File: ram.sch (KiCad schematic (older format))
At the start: 20 parts, among them U16 XX4256, U17 XX4256, U18 XX4256, U19 XX4256, U20 XX4256, U21 XX4256, U22 XX4256, U23 XX4256, U32 74LS139, U34 74LS373, U35 74LS244

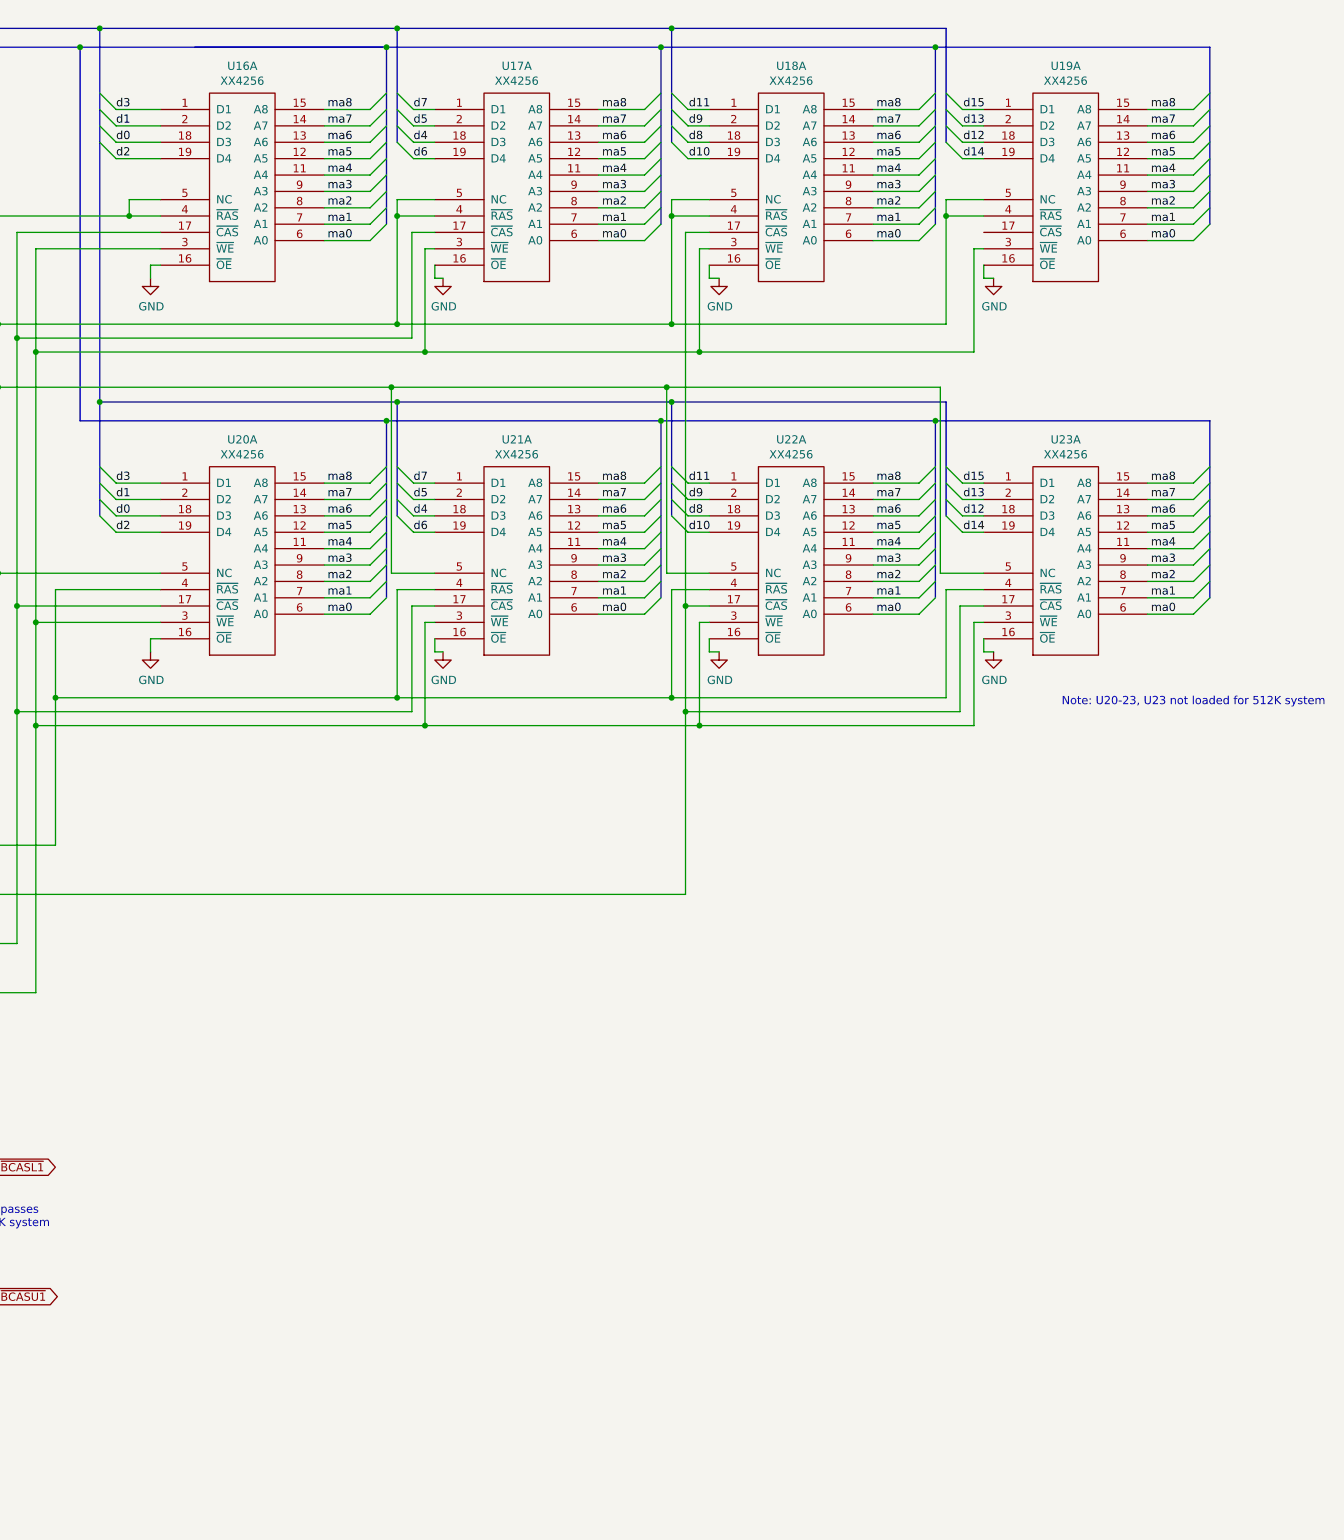
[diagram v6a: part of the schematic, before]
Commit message: Complete RAM
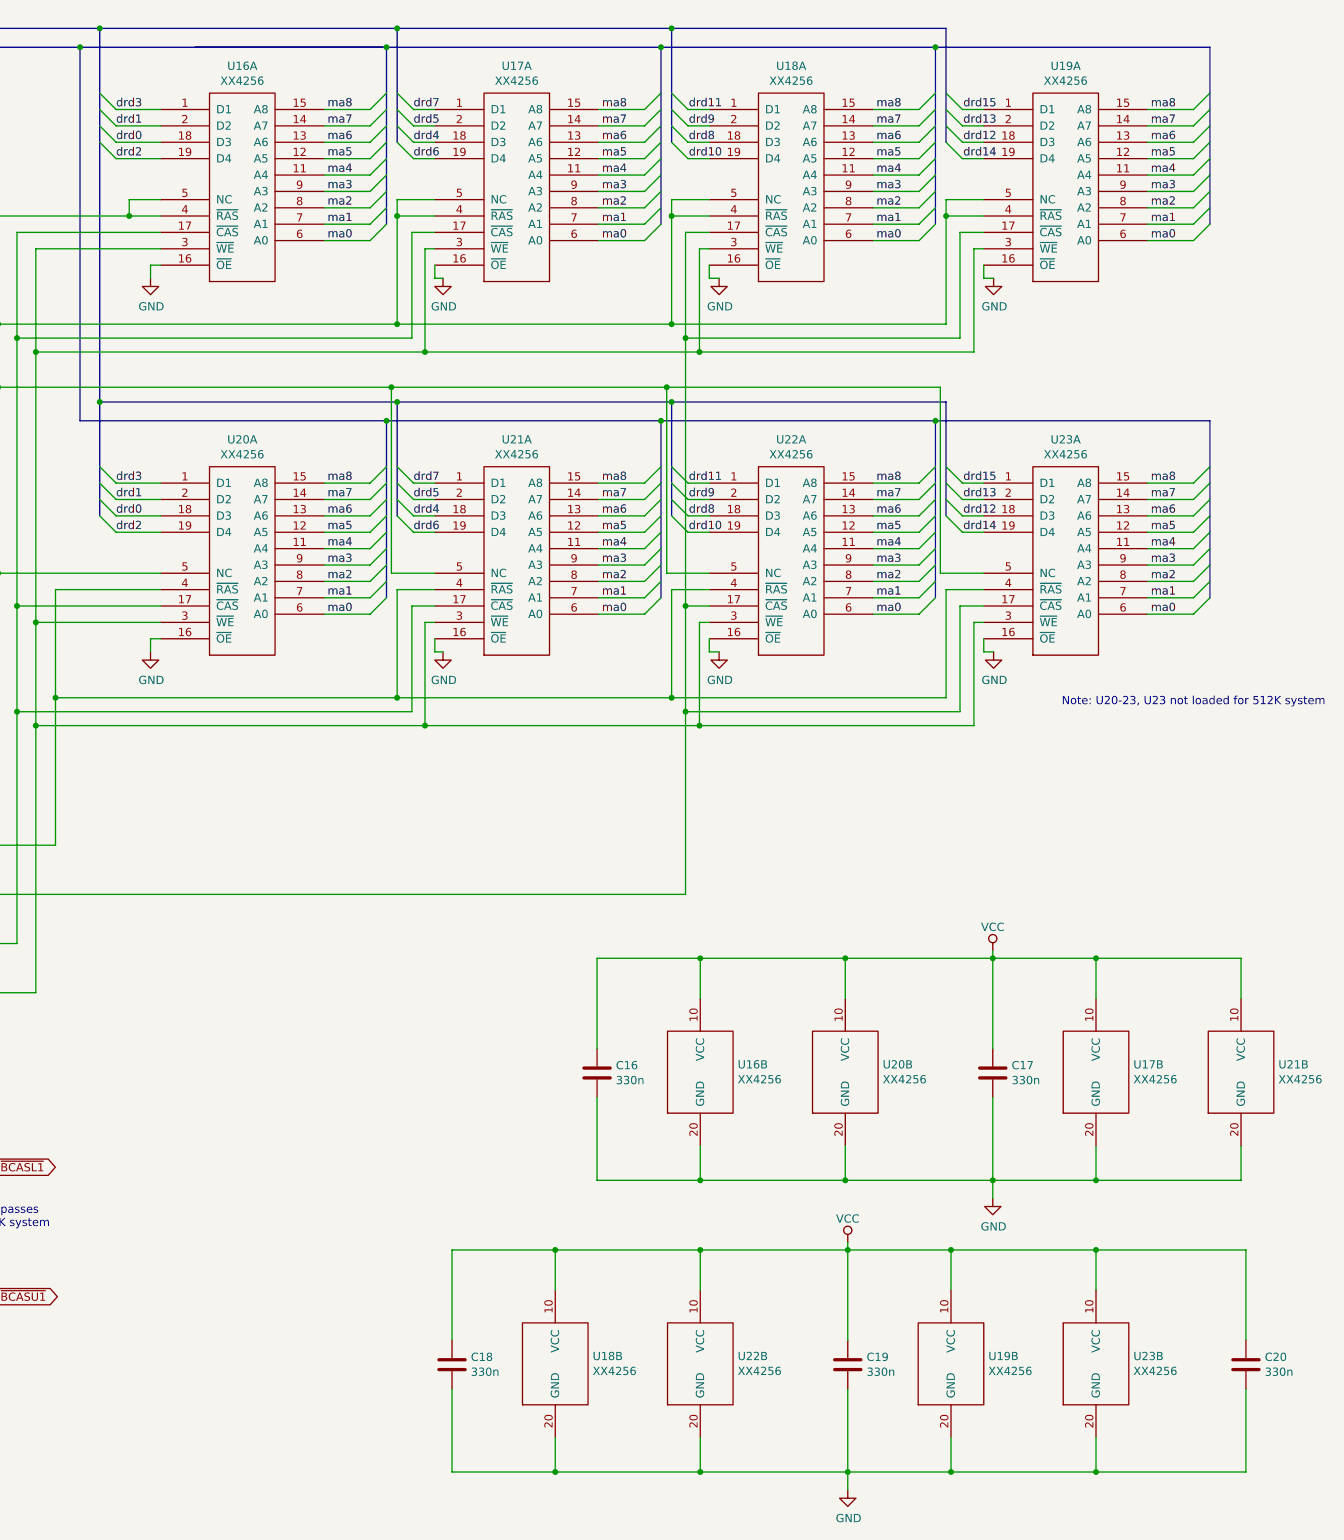
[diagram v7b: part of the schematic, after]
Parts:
- added C16, C17, C18, C19, C20: 330n, symbol Device:C
- added unit 2 of U16
- added unit 2 of U17
- added unit 2 of U18
- added unit 2 of U19
- added unit 2 of U20
- added unit 2 of U21
- added unit 2 of U22
- added unit 2 of U23
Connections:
- net GND: now also C16.2, C17.2, C18.2, C19.2, C20.2, U16.20 (GND), U17.20 (GND), U18.20 (GND), U19.20 (GND), U20.20 (GND), U21.20 (GND), U22.20 (GND), U23.20 (GND)
- net VCC: now also C16.1, C17.1, C18.1, C19.1, C20.1, U16.10 (VCC), U17.10 (VCC), U18.10 (VCC), U19.10 (VCC), U20.10 (VCC), U21.10 (VCC), U22.10 (VCC), U23.10 (VCC)
- net at RP203.6 (R3.2), U18.17 (~CAS), U22.17 (~CAS)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: now also U19.17 (~CAS)
- net d0 renamed drd0
- net d1 renamed drd1
- net d10 renamed drd10
- net d11 renamed drd11
- net d12 renamed drd12
- net d13 renamed drd13
- net d14 renamed drd14
- net d15 renamed drd15
- net d2 renamed drd2
- net d3 renamed drd3
- net d4 renamed drd4
- net d5 renamed drd5
- net d6 renamed drd6
- net d7 renamed drd7
- net d8 renamed drd8
- net d9 renamed drd9

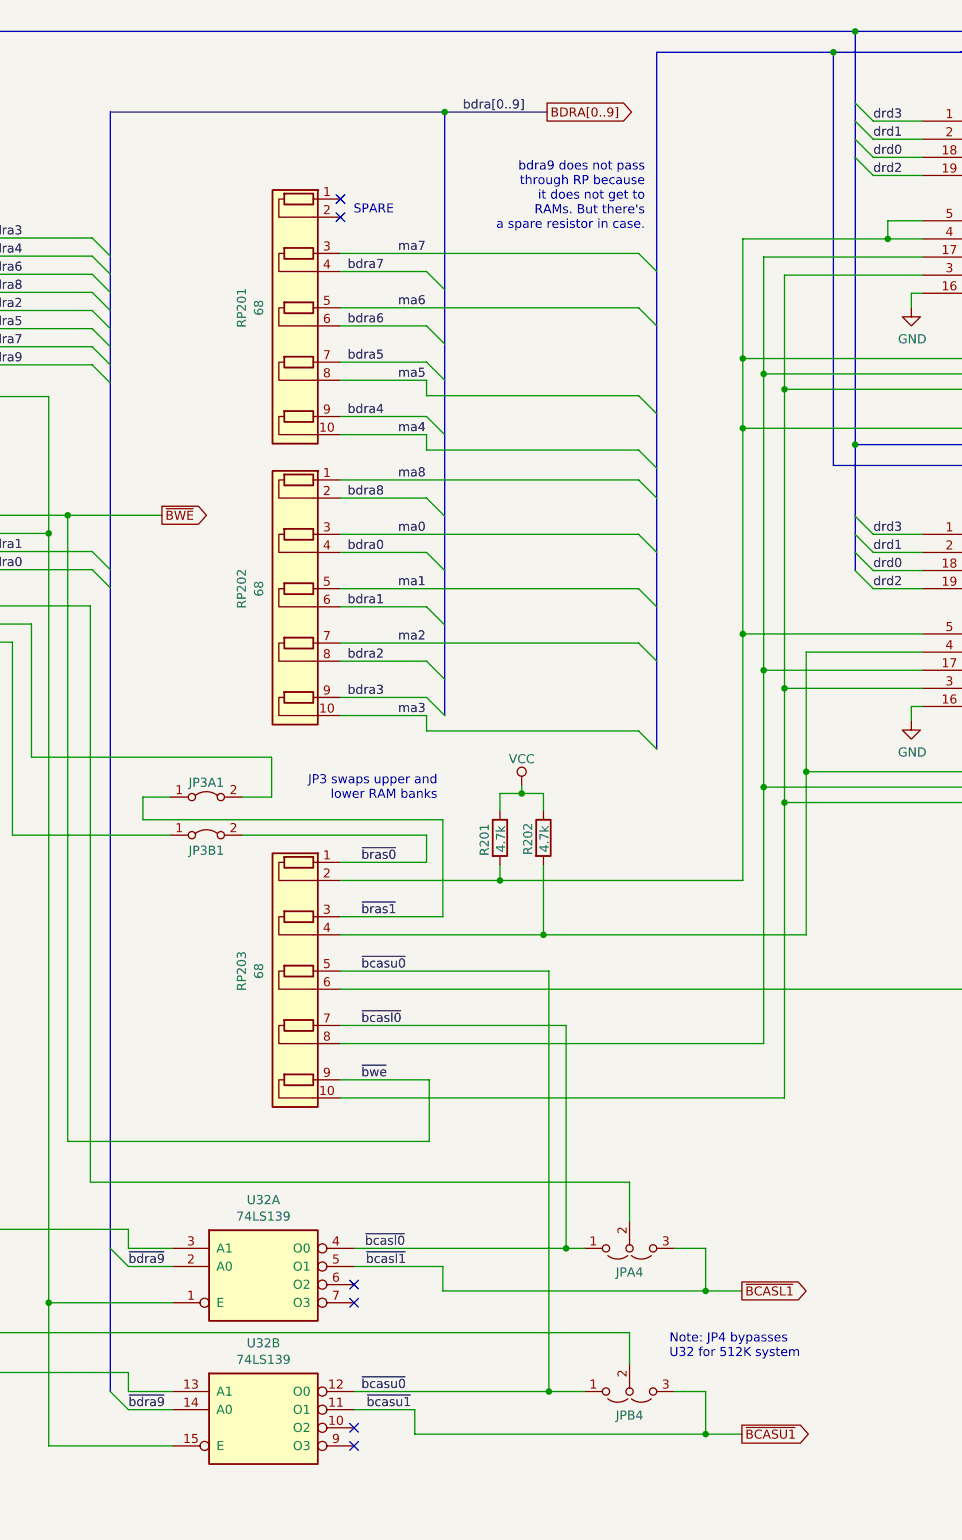
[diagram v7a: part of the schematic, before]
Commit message: Fix some RAM signals
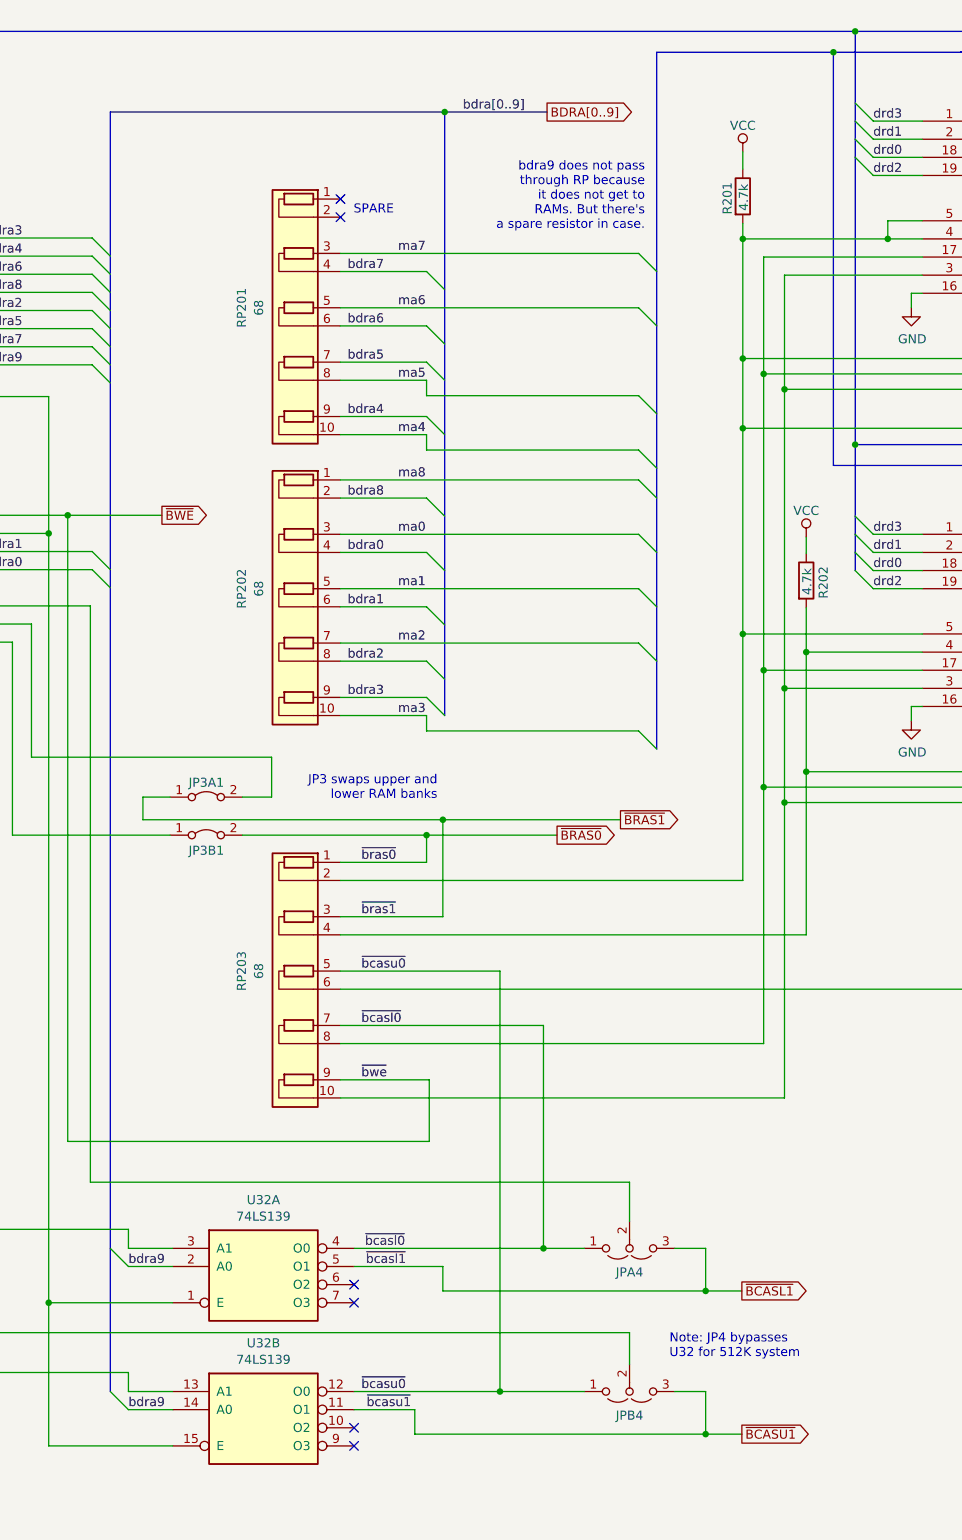
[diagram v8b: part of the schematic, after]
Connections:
- net ~bdra9 is gone; now on net bdra9: U32.14 (A0), U32.2 (A0)
- net ~bras0 renamed ~BRAS0
- net ~bras1 renamed ~BRAS1
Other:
- moved on the sheet: R201, R202
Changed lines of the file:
@@
 Wire Wire Line
 	6080 6540 5590 6540
-Wire Wire Line
-	5590 5740 6710 5740
-Wire Wire Line
-	5590 5440 6470 5440
 Text Label 5705 5940 0    50   ~ 0
 ~bcasu0
@@
 	4320 8260 4420 8360
 Text Label 4420 8360 0    50   ~ 0
-~bdra9
+bdra9
 Wire Wire Line
 	4665 7570 4420 7570
@@
 	4320 7470 4420 7570
 Text Label 4420 7570 0    50   ~ 0
-~bdra9
+bdra9
 Wire Wire Line
 	4665 7470 4420 7470
@@
 L Device:R R201
 U 1 1 5D708549
-P 6470 5205
-F 0 "R201" V 6385 5105 50  0000 L CNN
-F 1 "4.7k" V 6475 5125 50  0000 L CNN
-F 2 "Raemixx500:R_Axial_DIN0309_L9.0mm_D3.2mm_P12.70mm_Horizontal" V 6400 5205 50  0001 C CNN
-F 3 "~" H 6470 5205 50  0001 C CNN
-	1    6470 5205
+P 7810 1665
+F 0 "R201" V 7725 1565 50  0000 L CNN
+F 1 "4.7k" V 7815 1585 50  0000 L CNN
+F 2 "Raemixx500:R_Axial_DIN0309_L9.0mm_D3.2mm_P12.70mm_Horizontal" V 7740 1665 50  0001 C CNN
+F 3 "~" H 7810 1665 50  0001 C CNN
+	1    7810 1665
 	1    0    0    -1
 $EndComp
@@
 L Device:R R202
 U 1 1 5D708798
-P 6710 5205
-F 0 "R202" V 6625 5110 50  0000 L CNN
-F 1 "4.7k" V 6715 5125 50  0000 L CNN
-F 2 "Raemixx500:R_Axial_DIN0309_L9.0mm_D3.2mm_P12.70mm_Horizontal" V 6640 5205 50  0001 C CNN
-F 3 "~" H 6710 5205 50  0001 C CNN
-	1    6710 5205
-	1    0    0    -1
-$EndComp
-Wire Wire Line
-	6470 5355 6470 5440
-Connection ~ 6470 5440
-Wire Wire Line
-	6470 5440 7810 5440
-Wire Wire Line
-	6710 5355 6710 5740
-Connection ~ 6710 5740
-Wire Wire Line
-	6470 5055 6470 4960
-Wire Wire Line
-	6470 4960 6590 4960
-Wire Wire Line
-	6710 4960 6710 5055
+P 8160 3785
+F 0 "R202" V 8255 3685 50  0000 L CNN
+F 1 "4.7k" V 8165 3705 50  0000 L CNN
+F 2 "Raemixx500:R_Axial_DIN0309_L9.0mm_D3.2mm_P12.70mm_Horizontal" V 8090 3785 50  0001 C CNN
+F 3 "~" H 8160 3785 50  0001 C CNN
+	1    8160 3785
+	1    0    0    -1
+$EndComp
+Wire Wire Line
+	7810 1815 7810 1900
+Wire Wire Line
+	8160 3935 8160 4180
+Wire Wire Line
+	7810 1515 7810 1420
+Wire Wire Line
+	8160 3545 8160 3635
 $Comp
 L power:VCC #PWR0120
 U 1 1 5D7D48CC
-P 6590 4915
-F 0 "#PWR0120" H 6590 4765 50  0001 C CNN
-F 1 "VCC" H 6590 5060 50  0000 C CNN
-F 2 "" H 6590 4915 50  0001 C CNN
-F 3 "" H 6590 4915 50  0001 C CNN
-	1    6590 4915
-	1    0    0    -1
-$EndComp
-Wire Wire Line
-	6590 4915 6590 4960
-Connection ~ 6590 4960
-Wire Wire Line
-	6590 4960 6710 4960
+P 7810 1420
+F 0 "#PWR0120" H 7810 1270 50  0001 C CNN
+F 1 "VCC" H 7810 1565 50  0000 C CNN
+F 2 "" H 7810 1420 50  0001 C CNN
+F 3 "" H 7810 1420 50  0001 C CNN
+	1    7810 1420
+	1    0    0    -1
+$EndComp
 Text Label 5980 8360 2    50   ~ 0
 ~bcasu1
@@
 ~bcasu0
 Wire Wire Line
-	5590 5940 6740 5940
+	5590 5940 6470 5940
 Text Notes 7405 8080 0    50   ~ 0
 Note: JP4 bypasses\nU32 for 512K system
@@
 	8160 4180 8800 4180
 Wire Wire Line
-	6710 5740 8160 5740
-Wire Wire Line
 	10245 4840 8160 4840
 Connection ~ 10245 4840
 Connection ~ 8160 4840
-Wire Wire Line
-	8160 4840 8160 4180
 Wire Wire Line
 	8800 4080 7810 4080
@@
 	4210 3925 4210 7105
 Wire Wire Line
-	5590 6240 6835 6240
-Wire Wire Line
-	5665 7470 6835 7470
-Wire Wire Line
-	6835 6240 6835 7470
+	5590 6240 6710 6240
+Wire Wire Line
+	5665 7470 6710 7470
+Wire Wire Line
+	6710 6240 6710 7470
 Wire Wire Line
 	6155 7705 7605 7705
 Wire Wire Line
-	6835 7470 6935 7470
-Connection ~ 6835 7470
+	6710 7470 6935 7470
+Connection ~ 6710 7470
 Wire Wire Line
 	7185 7105 7185 7320
@@
 	7185 7935 7185 8110
 Wire Wire Line
-	6740 5940 6740 8260
-Wire Wire Line
-	5665 8260 6740 8260
-Connection ~ 6740 8260
-Wire Wire Line
-	6740 8260 6935 8260
+	6470 5940 6470 8260
+Wire Wire Line
+	5665 8260 6470 8260
+Connection ~ 6470 8260
+Wire Wire Line
+	6470 8260 6935 8260
 Text Notes 15910 4895 2    50   ~ 0
 Note: U20-23, U23 not loaded for 512K system
@@
 Wire Wire Line
 	13680 2645 12005 2645
+Connection ~ 12005 2645
+Wire Wire Line
+	12005 2645 12005 4280
+Connection ~ 7810 1900
+Wire Wire Line
+	5590 5440 7810 5440
+Wire Wire Line
+	8160 4840 8160 4180
+Connection ~ 8160 4180
+Wire Wire Line
+	5590 5740 8160 5740
+$Comp
+L power:VCC #PWR0114
+U 1 1 5D47A406
+P 8160 3545
+F 0 "#PWR0114" H 8160 3395 50  0001 C CNN
+F 1 "VCC" H 8160 3690 50  0000 C CNN
+F 2 "" H 8160 3545 50  0001 C CNN
+F 3 "" H 8160 3545 50  0001 C CNN
+	1    8160 3545
+	1    0    0    -1
+$EndComp
+Wire Wire Line
+	6065 5190 6785 5190
+Connection ~ 6065 5190
+Wire Wire Line
+	6155 5105 7135 5105
+Connection ~ 6155 5105
+Text GLabel 7135 5105 2    50   Output ~ 0
+~BRAS1
+Text GLabel 6785 5190 2    50   Output ~ 0
+~BRAS0
 Wire Bus Line
 	10245 755  10245 1450
@@
 Wire Bus Line
 	7335 870  7335 4715
-Connection ~ 12005 2645
-Wire Wire Line
-	12005 2645 12005 4280
 $EndSCHEMATC
